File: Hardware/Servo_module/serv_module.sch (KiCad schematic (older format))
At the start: 0 parts

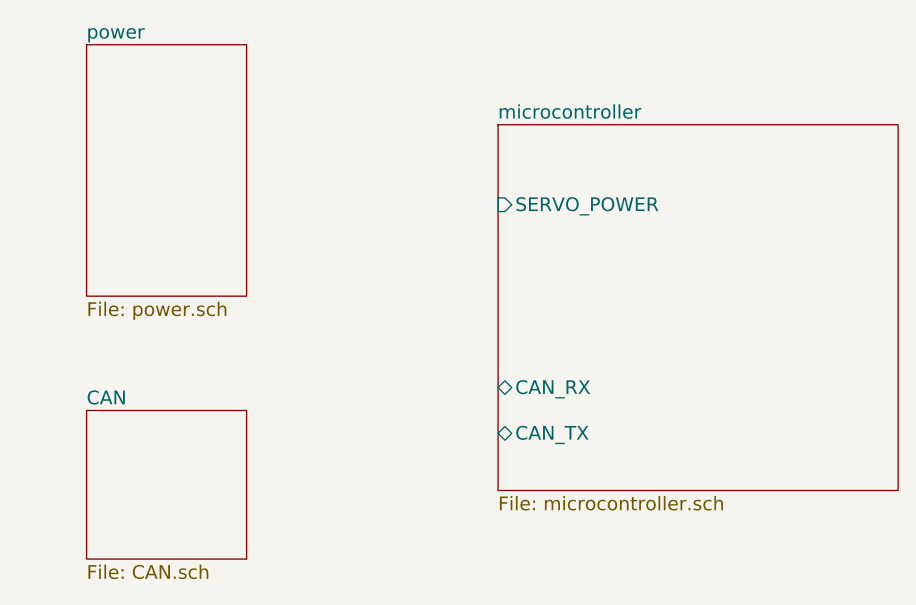
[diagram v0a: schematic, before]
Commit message: [HARDWARE][SERVO_MODULE] Schematic
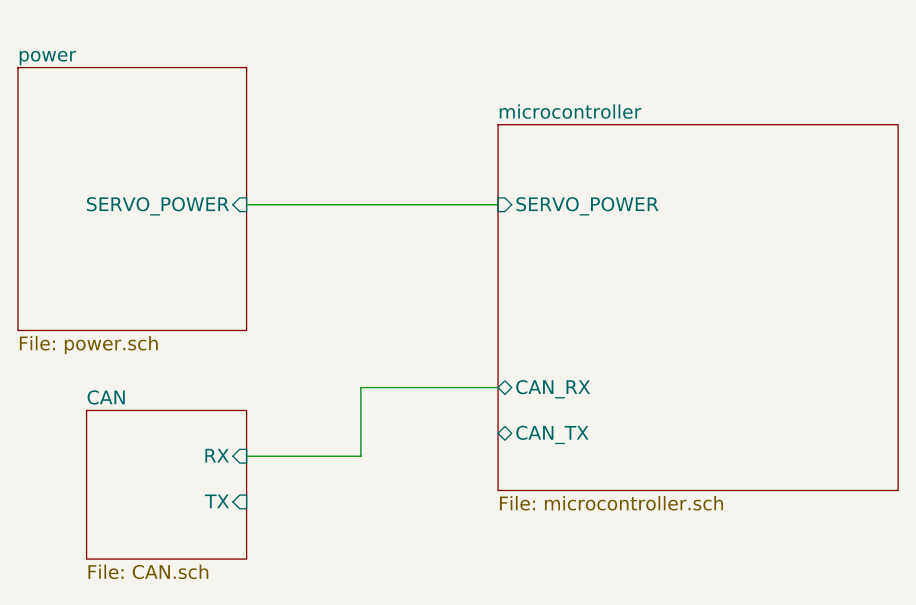
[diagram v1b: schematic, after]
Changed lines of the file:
@@
-EESchema Schematic File Version 2  date Fri 18 Oct 2013 03:55:12 PM CEST
+EESchema Schematic File Version 2
 LIBS:power
 LIBS:device
@@
 LIBS:conn_2_jst
 LIBS:conn_4_jst
+LIBS:sn65hvd232d
 LIBS:serv_module-cache
-EELAYER 24  0
+EELAYER 27 0
 EELAYER END
-$Descr A4 11700 8267
+$Descr A4 11693 8268
+encoding utf-8
 Sheet 1 4
 Title ""
-Date "18 oct 2013"
+Date "25 oct 2013"
 Rev ""
 Comp ""
@@
 $EndDescr
 $Sheet
-S 3450 2700 700  1100
+S 3150 2800 1000 1150
 U 526133C4
 F0 "power" 60
 F1 "power.sch" 60
+F2 "SERVO_POWER" I R 4150 3400 60
 $EndSheet
 $Sheet
@@
 F0 "CAN" 60
 F1 "CAN.sch" 60
+F2 "TX" I R 4150 4700 60
+F3 "RX" I R 4150 4500 60
 $EndSheet
 $Sheet
@@
 F4 "CAN_TX" B L 5250 4400 60
 $EndSheet
+Wire Wire Line
+	4150 4500 4650 4500
+Wire Wire Line
+	4650 4500 4650 4200
+Wire Wire Line
+	4650 4200 5250 4200
+Wire Wire Line
+	4150 3400 5250 3400
 $EndSCHEMATC

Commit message: [HARDWARE][SERVO_MODULE] Schematic
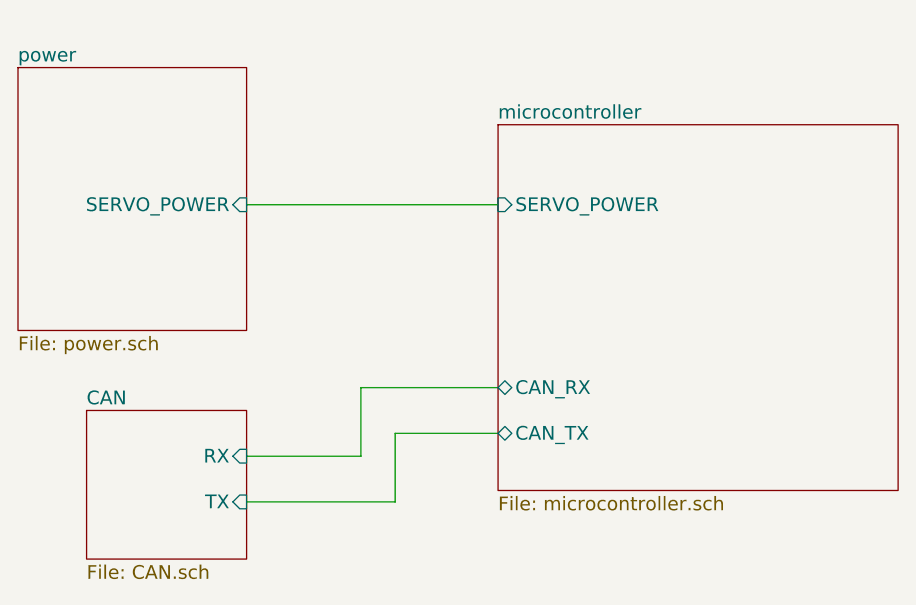
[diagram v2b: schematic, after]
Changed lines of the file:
@@
 Wire Wire Line
 	4150 3400 5250 3400
+Wire Wire Line
+	4150 4700 4800 4700
+Wire Wire Line
+	4800 4700 4800 4400
+Wire Wire Line
+	4800 4400 5250 4400
 $EndSCHEMATC

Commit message: [HARDWARE][SERVO_MODULE] Update schemating & routing
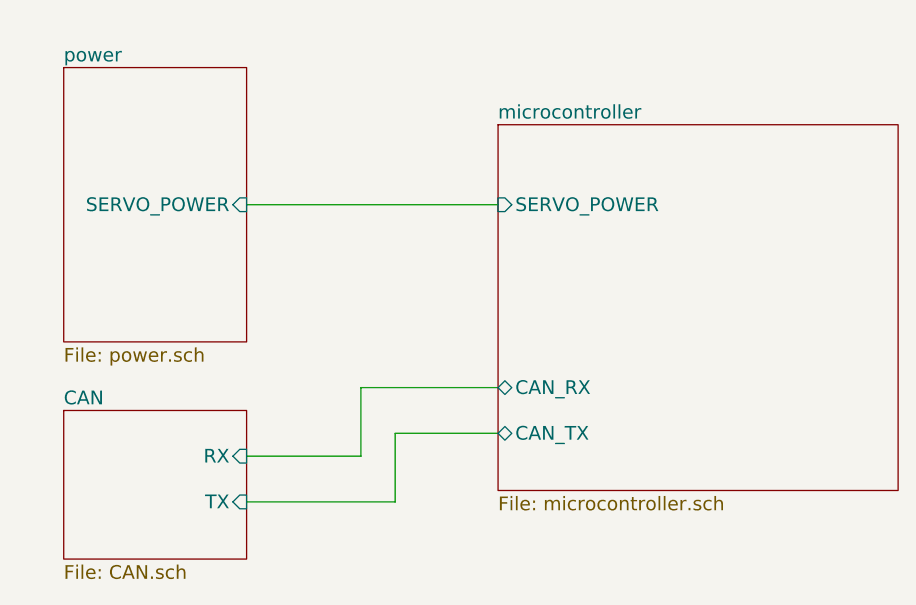
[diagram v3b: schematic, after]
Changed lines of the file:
@@
 LIBS:contrib
 LIBS:valves
-LIBS:stm32f103c4
 LIBS:ap1117
 LIBS:conn_2_jst
 LIBS:conn_4_jst
 LIBS:sn65hvd232d
+LIBS:stm32f103c4
 LIBS:serv_module-cache
 EELAYER 27 0
@@
 $EndDescr
 $Sheet
-S 3150 2800 1000 1150
-U 526133C4
-F0 "power" 60
-F1 "power.sch" 60
-F2 "SERVO_POWER" I R 4150 3400 60
-$EndSheet
-$Sheet
-S 3450 4300 700  650
+S 3350 4300 800  650
 U 52612DF7
 F0 "CAN" 60
@@
 Wire Wire Line
 	4800 4400 5250 4400
+$Sheet
+S 3350 2800 800  1200
+U 526133C4
+F0 "power" 60
+F1 "power.sch" 60
+F2 "SERVO_POWER" I R 4150 3400 60
+$EndSheet
 $EndSCHEMATC
